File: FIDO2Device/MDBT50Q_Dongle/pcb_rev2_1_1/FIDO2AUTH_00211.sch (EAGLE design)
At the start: 40 parts, among them CN1 TE-1734028, CN2 IF_4PIN, CN3 IF_2PIN_SOL, CN5 IF_2PIN_SOL, SW1 SKRPACE010, SW2 SKTADAE010, U1 MDBT50Q-P1M, U2 XC6206P332MR-G, U3 ATECC608A-MAHDA-S, X1 NX3215SA-32.768K

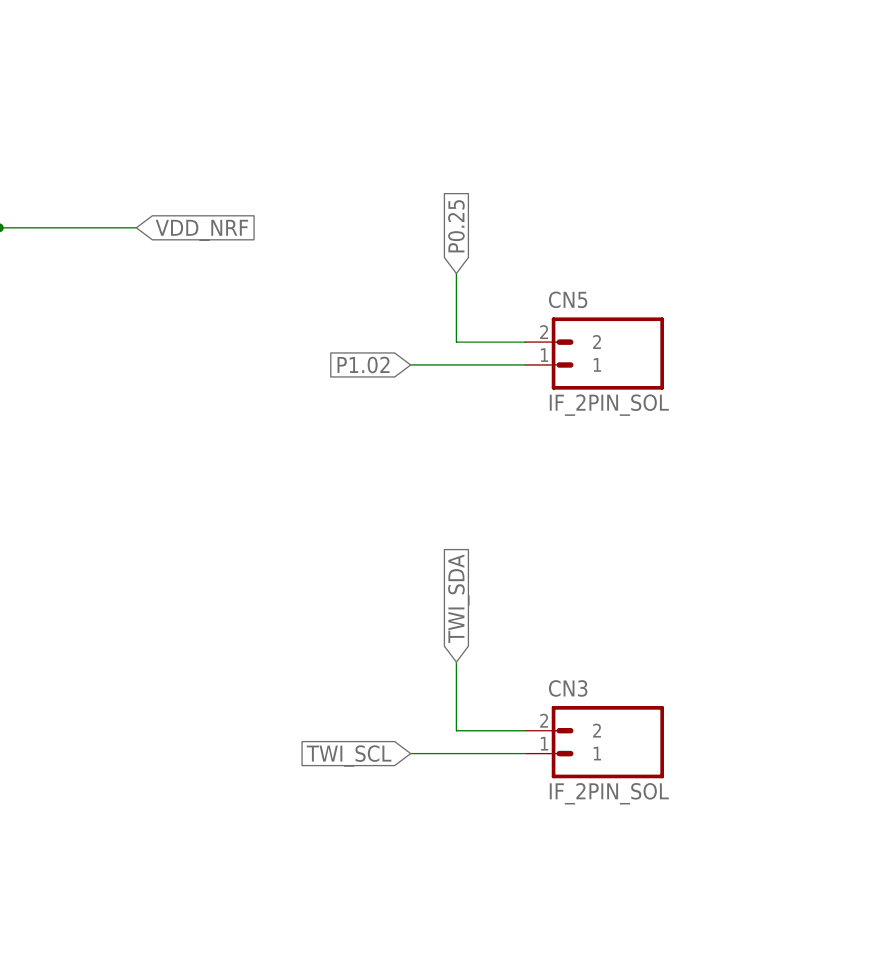
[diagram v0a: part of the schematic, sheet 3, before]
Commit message: プリント基板設計データを修正
・セキュアIC関連部品を搭載したパターンを作成
・TWI用のブレークアウトパターンを削除
・ATECC608Aの底面パッドパターンを削除
（ICの背面で配線する必要があるための措置）
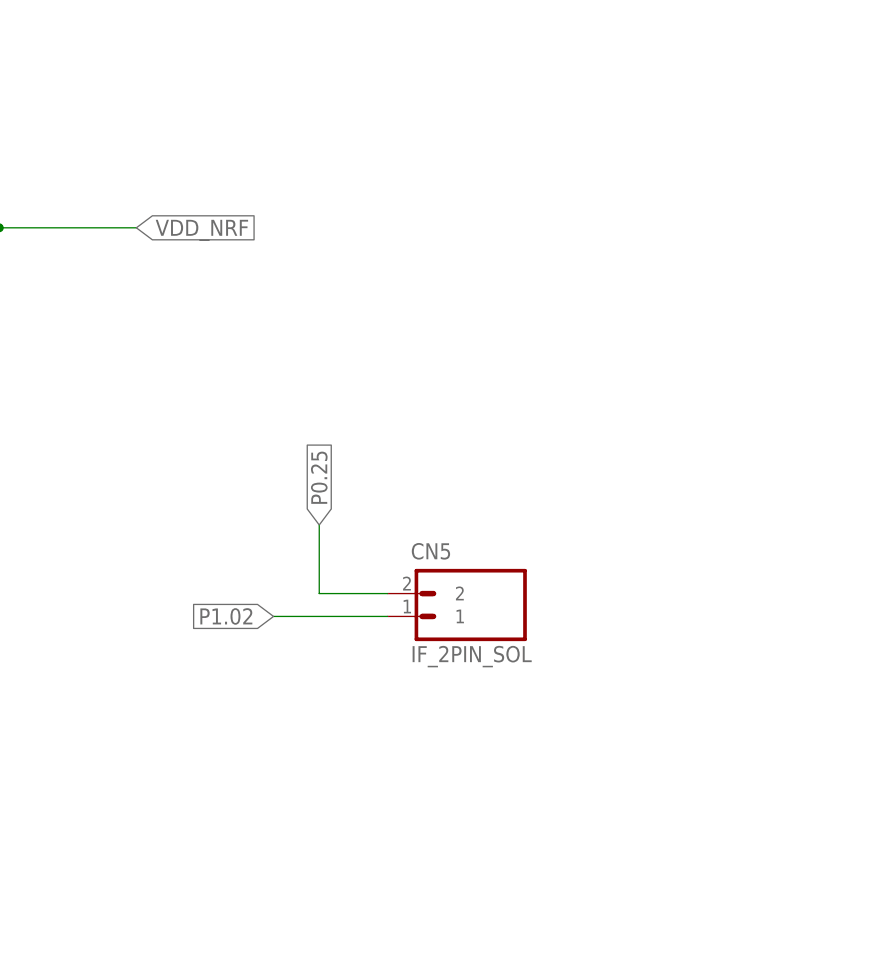
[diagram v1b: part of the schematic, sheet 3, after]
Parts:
- removed CN3: IF_2PIN_SOL, Connectors:IF_2PIN_SOL
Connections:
- net 0V: no longer U3.EXP
- net TWI_SCL: no longer CN3.1
- net TWI_SDA: no longer CN3.2
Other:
- moved on the sheet: CN5
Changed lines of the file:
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@@
 <part name="CN2" library="Connectors" deviceset="IF_4PIN" device=""/>
 <part name="CN5" library="Connectors" deviceset="IF_2PIN" device="_SOL" value="IF_2PIN_SOL"/>
-<part name="CN3" library="Connectors" deviceset="IF_2PIN" device="_SOL"/>
 <part name="U3" library="ICs" deviceset="ATECC608A" device="-MAHDA-S"/>
 <part name="GND19" library="Supply" deviceset="0V" device=""/>
@@
 <instance part="BAT1" gate="G$1" x="93.98" y="81.28"/>
 <instance part="GND18" gate="1" x="66.04" y="71.12"/>
-<instance part="CN5" gate="G$1" x="203.2" y="111.76"/>
-<instance part="CN3" gate="G$1" x="203.2" y="68.58"/>
+<instance part="CN5" gate="G$1" x="187.96" y="83.82"/>
 </instances>
 <busses>
@@
 </segment>
 </net>
-<net name="TWI_SDA" class="0">
-<segment>
-<wire x1="195.58" y1="68.58" x2="195.58" y2="76.2" width="0.1524" layer="91"/>
-<label x="195.58" y="76.2" size="1.778" layer="95" rot="R90" xref="yes"/>
-<pinref part="CN3" gate="G$1" pin="2"/>
-<wire x1="203.2" y1="68.58" x2="195.58" y2="68.58" width="0.1524" layer="91"/>
-</segment>
-</net>
-<net name="TWI_SCL" class="0">
-<segment>
-<label x="190.5" y="66.04" size="1.778" layer="95" rot="R180" xref="yes"/>
-<pinref part="CN3" gate="G$1" pin="1"/>
-<wire x1="203.2" y1="66.04" x2="190.5" y2="66.04" width="0.1524" layer="91"/>
-</segment>
-</net>
 <net name="P0.25" class="0">
 <segment>
-<wire x1="195.58" y1="111.76" x2="195.58" y2="119.38" width="0.1524" layer="91"/>
-<label x="195.58" y="119.38" size="1.778" layer="95" rot="R90" xref="yes"/>
+<wire x1="180.34" y1="83.82" x2="180.34" y2="91.44" width="0.1524" layer="91"/>
+<label x="180.34" y="91.44" size="1.778" layer="95" rot="R90" xref="yes"/>
 <pinref part="CN5" gate="G$1" pin="2"/>
-<wire x1="203.2" y1="111.76" x2="195.58" y2="111.76" width="0.1524" layer="91"/>
+<wire x1="187.96" y1="83.82" x2="180.34" y2="83.82" width="0.1524" layer="91"/>
 </segment>
 </net>
 <net name="P1.02" class="0">
 <segment>
-<label x="190.5" y="109.22" size="1.778" layer="95" rot="R180" xref="yes"/>
+<label x="175.26" y="81.28" size="1.778" layer="95" rot="R180" xref="yes"/>
 <pinref part="CN5" gate="G$1" pin="1"/>
-<wire x1="190.5" y1="109.22" x2="203.2" y2="109.22" width="0.1524" layer="91"/>
+<wire x1="175.26" y1="81.28" x2="187.96" y2="81.28" width="0.1524" layer="91"/>
 </segment>
 </net>
@@
 <net name="0V" class="0">
 <segment>
-<pinref part="U3" gate="G$1" pin="EXP"/>
 <pinref part="GND19" gate="1" pin="0V"/>
-<wire x1="99.06" y1="83.82" x2="91.44" y2="83.82" width="0.1524" layer="91"/>
-<wire x1="91.44" y1="83.82" x2="91.44" y2="73.66" width="0.1524" layer="91"/>
+<wire x1="91.44" y1="88.9" x2="91.44" y2="73.66" width="0.1524" layer="91"/>
 <pinref part="U3" gate="G$1" pin="GND"/>
 <wire x1="99.06" y1="88.9" x2="91.44" y2="88.9" width="0.1524" layer="91"/>
-<wire x1="91.44" y1="88.9" x2="91.44" y2="83.82" width="0.1524" layer="91"/>
-<junction x="91.44" y="83.82"/>
-</segment>
-<segment>
+</segment>
+<segment>

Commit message: プリント基板設計データを修正
・チップコンデンサー／フェライトビーズのパッドパターン間隔を拡張
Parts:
- C12, C5, C7, C8, C9: device Parts:CAP_0402 -> Parts:CAP_0402K
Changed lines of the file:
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@@
 <setting verticaltext="up"/>
 </settings>
-<grid distance="0.1" unitdist="inch" unit="inch" style="lines" multiple="1" display="yes" altdistance="0.01" altunitdist="inch" altunit="inch"/>
+<grid distance="0.1" unitdist="inch" unit="inch" style="lines" multiple="1" display="no" altdistance="0.01" altunitdist="inch" altunit="inch"/>
 <layers>
 <layer number="1" name="Top" color="4" fill="1" visible="no" active="no"/>
@@
 <part name="FB1" library="Parts" deviceset="BLM15AG" device="121SN1D"/>
 <part name="FB2" library="Parts" deviceset="BLM15AG" device="121SN1D"/>
-<part name="C5" library="Parts" deviceset="CAP" device="_0402" value="0.01uF"/>
+<part name="C5" library="Parts" deviceset="CAP" device="_0402K" value="0.01uF"/>
 <part name="C6" library="Parts" deviceset="CAP" device="_0603" value="10uF"/>
-<part name="C7" library="Parts" deviceset="CAP" device="_0402" value="0.1uF"/>
-<part name="C8" library="Parts" deviceset="CAP" device="_0402" value="0.1uF"/>
+<part name="C7" library="Parts" deviceset="CAP" device="_0402K" value="0.1uF"/>
+<part name="C8" library="Parts" deviceset="CAP" device="_0402K" value="0.1uF"/>
 <part name="GND8" library="Supply" deviceset="0V" device=""/>
 <part name="GND9" library="Supply" deviceset="0V" device=""/>
@@
 <part name="CN1" library="Connectors" deviceset="TE-1734028" device=""/>
 <part name="R1" library="Parts" deviceset="RESISTOR" device="_0402" value="10k"/>
-<part name="C9" library="Parts" deviceset="CAP" device="_0402" value="0.1uF"/>
+<part name="C9" library="Parts" deviceset="CAP" device="_0402K" value="0.1uF"/>
 <part name="GND11" library="Supply" deviceset="0V" device=""/>
 <part name="SW1" library="Parts" deviceset="SKRPACE010" device=""/>
@@
 <part name="U3" library="ICs" deviceset="ATECC608A" device="-MAHDA-S"/>
 <part name="GND19" library="Supply" deviceset="0V" device=""/>
-<part name="C12" library="Parts" deviceset="CAP" device="_0402" value="0.1uF"/>
+<part name="C12" library="Parts" deviceset="CAP" device="_0402K" value="0.1uF"/>
 <part name="GND20" library="Supply" deviceset="0V" device=""/>
 <part name="R7" library="Parts" deviceset="RESISTOR" device="_0402" value="3.6k"/>
